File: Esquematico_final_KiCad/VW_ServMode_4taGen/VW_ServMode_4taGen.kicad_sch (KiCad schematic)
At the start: 33 parts, among them J1 MicroSDReader, J2 USB-C, J3 ClampConnections, J4 uC_custom, J5 TP4056_Custom_2extraOutputs, J6 3v3Switch, SW1 SW_In, SW2 SW_Out, SW3 SW_Reset

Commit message: - Esquematico actualizado - PCB enrutado
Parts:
- removed AFF2: LTS-6980HR, Display_7Segment:7SegmentLED_LTS6760_LTS6780, symbol Display_Character:LTS-6980HR
- removed D8: LED_ModServOn, symbol Device:LED
- removed D9: LED_ModServOff, symbol Device:LED
- removed J1: MicroSDReader, Connector_Wire:SolderWire-2sqmm_1x06_P7.8mm_D2mm_OD3.9mm, symbol Connector_Generic:Conn_01x06
- removed J2: USB-C, symbol Connector_Generic:Conn_01x04
- removed J3: ClampConnections, Connector_Hirose:Hirose_DF11-8DP-2DSA_2x04_P2.00mm_Vertical, symbol Connector_Generic:Conn_02x04_Counter_Clockwise
- removed J4: uC_custom, symbol Connector_Generic:Conn_02x15_Counter_Clockwise
- removed J5: TP4056_Custom_2extraOutputs, symbol Connector_Generic:Conn_02x04_Counter_Clockwise
- removed J6: 3v3Switch, symbol Connector_Generic:Conn_01x03
- removed SW3: SW_Reset, symbol Switch:SW_Push
- added AFF1: LTS-6960HR, Display_7Segment:7SegmentLED_LTS6760_LTS6780, symbol Display_Character:LTS-6960HR
- added BAR1: HDSP-4830_2, Display:HDSP-4830, symbol LED:HDSP-4830_2
- added BT1: Battery, Battery:BatteryHolder_Keystone_1042_1x18650, symbol Device:Battery_Cell
- added C1, C10, C11, C12, C15, C18, C2, C21, C22, C4, C6, C8: C100N, Capacitor_SMD:C_0603_1608Metric, symbol Device:C
- added C13, C14, C3, C5, C7, C9: C10U, Capacitor_SMD:C_0603_1608Metric, symbol Device:C
- added C16, C17: C4U7, Capacitor_SMD:C_0603_1608Metric, symbol Device:C
- added C19, C20: C20P, Capacitor_SMD:C_0603_1608Metric, symbol Device:C
- added H1, H2, H3, H4: MountingHole, MountingHole:MountingHole_3.2mm_M3, symbol Mechanical:MountingHole
- added J1: Conn_02x03_Counter_Clockwise, Connector_PinHeader_2.54mm:PinHeader_2x03_P2.54mm_Vertical, symbol Connector_Generic:Conn_02x03_Counter_Clockwise
- added J10: Micro_SD_Card, Own-Footprints:MicroSD_Memory, symbol Connector:Micro_SD_Card
- added J11: USB_C_Receptacle_USB2.0_14P, Connector_USB:USB_C_Receptacle_G-Switch_GT-USB-7010ASV, symbol Connector:USB_C_Receptacle_USB2.0_14P
- added J12: Conn_02x04_Counter_Clockwise, Connector_IDC:IDC-Header_2x04_P2.54mm_Horizontal, symbol Connector_Generic:Conn_02x04_Counter_Clockwise
- added J2: Conn_01x04_Pin, Connector_PinHeader_2.54mm:PinHeader_1x04_P2.54mm_Vertical, symbol Connector:Conn_01x04_Pin
- added J3, J4, J5, J6, J7: Conn_01x02_Pin, Connector_PinHeader_2.54mm:PinHeader_1x02_P2.54mm_Vertical, symbol Connector:Conn_01x02_Pin
- added Q1: IRLML6402, Package_TO_SOT_SMD:SOT-23, symbol Transistor_FET:IRLML6402
- added R1: R5K1, Resistor_SMD:R_0603_1608Metric, symbol Device:R
- added R12: R4K7, Resistor_SMD:R_0603_1608Metric, symbol Device:R
- added R15: R2K2, Resistor_SMD:R_0603_1608Metric, symbol Device:R
- added R21, R22, R23, R24, R25, RB1, RC1, RD1, RE1, RF1, RG1: R330, Resistor_SMD:R_0603_1608Metric, symbol Device:R
- added R26: R5K, Resistor_SMD:R_0603_1608Metric, symbol Device:R
- added R27: R15K, Resistor_SMD:R_0603_1608Metric, symbol Device:R
- added R30, R6, R7, R8, R9: R10K, Resistor_SMD:R_0603_1608Metric, symbol Device:R
- added R31, R32: R100K, Resistor_SMD:R_0603_1608Metric, symbol Device:R
- added R4: R1K, Resistor_SMD:R_0603_1608Metric, symbol Device:R
- added R5: R1K2, Resistor_SMD:R_0603_1608Metric, symbol Device:R
- added SW4: SW_Out, Button_Switch_SMD:SW_SPST_Omron_B3FS-105xP, symbol Switch:SW_Push
- added U1: TP4056, Package_SO:SOIC-8-1EP_3.9x4.9mm_P1.27mm_EP2.29x3mm, symbol tp4056:TP4056
- added U2: DW01, Package_TO_SOT_SMD:SOT-23-6_Handsoldering, symbol dw01:DW01
- added U3: FS8205A, Package_SO:TSSOP-8_4.4x3mm_P0.65mm, symbol fs8205:FS8205A
- added U4: AMS1117-3.3, Package_TO_SOT_SMD:SOT-223-3_TabPin2, symbol Regulator_Linear:AMS1117-3.3
- added U5: STM32F103C6Tx, Package_QFP:LQFP-48_7x7mm_P0.5mm, symbol MCU_ST_STM32F1:STM32F103C6Tx
- added Y1: Crystal, Crystal:Crystal_SMD_ECS_CSM3X-2Pin_7.6x4.1mm, symbol Device:Crystal
- D1: value LED_BAT25 -> PC13; footprint (none) -> LED_SMD:LED_0805_2012Metric
- D2: value LED_BAT50 -> BAT25; footprint (none) -> LED_THT:LED_D5.0mm
- D3: value LED_BAT75 -> BAT50; footprint (none) -> LED_THT:LED_D5.0mm
- D4: value LED_BAT99 -> BAT75; footprint (none) -> LED_THT:LED_D5.0mm
- D5: value LED_OK -> BAT99; footprint (none) -> LED_THT:LED_D5.0mm
- D6: value LED_ERROR -> LED; footprint (none) -> LED_THT:LED_D5.0mm
- D7: value LED_BAT0 -> LED; footprint (none) -> LED_THT:LED_D5.0mm
- R10, R11: value 1k -> R10K; footprint (none) -> Resistor_SMD:R_0603_1608Metric
- R13: value 330 -> R4K7; footprint (none) -> Resistor_SMD:R_0603_1608Metric
- R14: value 330 -> R47K; footprint (none) -> Resistor_SMD:R_0603_1608Metric
- R16: renamed from R12; value 330 -> R330; footprint (none) -> Resistor_SMD:R_0603_1608Metric
- R17: renamed from R4; value 330 -> R330; footprint (none) -> Resistor_SMD:R_0603_1608Metric
- R18: renamed from R5; value 330 -> R330; footprint (none) -> Resistor_SMD:R_0603_1608Metric
- R19: renamed from R6; value 330 -> R330; footprint (none) -> Resistor_SMD:R_0603_1608Metric
- R2: value 330 -> R5K1; footprint (none) -> Resistor_SMD:R_0603_1608Metric
- R20: renamed from R7; value 330 -> R330; footprint (none) -> Resistor_SMD:R_0603_1608Metric
- R28: renamed from R8; value 330 -> R10K; footprint (none) -> Resistor_SMD:R_0603_1608Metric
- R29: renamed from R9; value 330 -> R10K; footprint (none) -> Resistor_SMD:R_0603_1608Metric
- R3: value 330 -> R1K; footprint (none) -> Resistor_SMD:R_0603_1608Metric
- RA1: renamed from R1; value 330 -> R330; footprint (none) -> Resistor_SMD:R_0603_1608Metric
- SW1, SW2: footprint (none) -> Button_Switch_SMD:SW_SPST_Omron_B3FS-105xP
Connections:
- net LED_B0 is gone; now on net +5V: D7.2 (A)
- net SCL is gone; now on net +3V3: R10.2
- net SDA is gone; now on net +3V3: R11.2
- net +5V: now also D6.2 (A), C11.2, C3.2, C4.2, J11.A4 (VBUS), J11.A9 (VBUS), J11.B4 (VBUS), J11.B9 (VBUS), J4.1 (Pin_1), J6.1 (Pin_1), U1.4 (VCC), U1.8 (CE)
- net GND: now also R2.1, R29.1, C1.1, C10.1, C11.1, C13.1, C14.1, C15.1, C16.1, C18.1, C19.1, C2.1, C20.1, C3.1, C4.1, C5.1, C6.1, C7.1, C8.1, C9.1, J1.5 (Pin_5), J1.6 (Pin_6), J10.6 (VSS), J11.A1 (GND), J11.A12 (GND), J11.B1 (GND), J11.B12 (GND), J12.4 (Pin_4), J2.4 (Pin_4), J4.2 (Pin_2), J5.2 (Pin_2), J6.2 (Pin_2), J7.2 (Pin_2), R1.2, R22.2, R23.2, R24.2, R25.2, R27.1, R5.1, SW4.1, U1.1 (TEMP), U1.3 (GND), U4.1 (GND), U5.23 (VSS), U5.35 (VSS), U5.47 (VSS), U5.8 (VSSA); no longer R13.2, R14.2, R2.2, R29.2, R3.2, RA1.1
- net LED_A: now also RA1.2, U5.14 (PA4)
- net LED_B: now also RB1.2, U5.13 (PA3)
- net LED_B25: now also BAR1.7 (A), BAR1.8 (A), U5.21 (PB10); no longer D1.2 (A)
- net LED_B50: now also BAR1.5 (A), BAR1.6 (A), U5.22 (PB11); no longer D2.2 (A)
- net LED_B75: now also BAR1.3 (A), BAR1.4 (A), U5.29 (PA8); no longer D3.2 (A)
- net LED_B99: now also BAR1.1 (A), BAR1.2 (A), U5.30 (PA9); no longer D4.2 (A)
- net LED_C: now also RC1.2, U5.10 (PA0)
- net LED_D: now also RD1.2, U5.12 (PA2)
- net LED_E: now also RE1.2, U5.11 (PA1)
- net LED_ERROR: now also D3.2 (A), U5.25 (PB12); no longer D6.2 (A)
- net LED_F: now also RF1.2, U5.40 (PB4)
- net LED_G: now also RG1.2, U5.39 (PB3)
- net LED_OK: now also D2.2 (A), U5.26 (PB13); no longer D5.2 (A)
- net TP_B-: now also BT1.2 (-), C12.1, U2.6 (GND), U3.2 (S1), U3.3 (S1)
- net CONN_SCL: now reaches R13.1
- net CONN_SCL: now also J12.6 (Pin_6), U5.42 (PB6)
- net at D5.1 (K): now also R25.1; no longer R2.1
- net at R14.1: now also C17.1, Q1.1 (G), R15.1
- net at R16.1: now also BAR1.11 (K), BAR1.12 (K); no longer D7.1 (K)
- net at R18.1: now also BAR1.15 (K), BAR1.16 (K); no longer D2.1 (K)
- net SD_CS: now reaches R11.1
- net SD_CS: now also J10.2 (DAT3/CD), U5.4 (PC15); no longer R10.1
- net at D6.1 (K): now also R3.2; no longer R3.1
- net at R19.1: now also BAR1.17 (K), BAR1.18 (K); no longer D3.1 (K)
- net at R17.1: now also BAR1.13 (K), BAR1.14 (K); no longer D1.1 (K)
- net at R20.1: now also BAR1.19 (K), BAR1.20 (K); no longer D4.1 (K)
- net +3.3V renamed +3V3
- net +3V3: now also D1.2 (A), R14.2, AFF1.3 (C.A.), AFF1.8 (C.A.), C1.2, C10.2, C14.2, C15.2, C17.2, C2.2, C21.2, C22.2, C5.2, C6.2, C9.2, J1.1 (Pin_1), J1.2 (Pin_2), J10.4 (VDD), J2.1 (Pin_1), J5.1 (Pin_1), J7.1 (Pin_1), Q1.2 (S), R30.2, R8.2, R9.2, U4.2 (VO), U5.24 (VDD), U5.36 (VDD), U5.48 (VDD), U5.9 (VDDA)
- net Push_In renamed PUSH_IN
- net PUSH_IN: now also C21.1, U5.28 (PB15)
- net Push_Out renamed PUSH_OUT
- net PUSH_OUT: now also R29.2, C22.1, U5.27 (PB14); no longer R29.1
- new net: AFF1.4 (c), RC1.1
- new net: AFF1.1 (e), RE1.1
- new net: AFF1.10 (g), RG1.1
- new net: AFF1.2 (d), RD1.1
- new net: AFF1.6 (b), RB1.1
- new net: AFF1.7 (a), RA1.1
- new net: AFF1.9 (f), RF1.1
- new net: D2.1 (K), R22.1
- new net: J11.A5 (CC1), R1.1
- new net: D4.1 (K), R24.1
- new net: R5.2, U1.2 (PROG)
- new net: J11.B5 (CC2), R2.2
- new net: D7.1 (K), R4.2
- new net: R6.1, U3.6 (S2), U3.7 (S2)
- new net: R6.2, U2.2 (CS)
- new net: U2.1 (OD), U3.4 (G1)
- new net: U2.3 (OC), U3.5 (G2)
- new net: C12.2, R7.2, U2.5 (VCC)
- new net: R31.1, U5.44 (BOOT0)
- new net: D3.1 (K), R23.1
- new net: D1.1 (K), R21.1
- new net #RESET: R30.1, SW4.2, U5.7 (NRST)
- new net BAT+: BT1.1 (+), C13.2, J3.2 (Pin_2), R26.2, R7.1, U1.5 (BAT)
- new net BAT_LVL: C18.2, R26.1, R27.2, U5.18 (PB0)
- new net BOOT0: J1.3 (Pin_3), R31.2
- new net BOOT1: J1.4 (Pin_4), R32.2
- new net CONN_SDA: J12.5 (Pin_5), R12.1, U5.43 (PB7)
- new net DCLK: J2.3 (Pin_3), U5.37 (PA14)
- new net DIO: J2.2 (Pin_2), U5.34 (PA13)
- new net DO_3V3: C16.2, J12.8 (Pin_8), Q1.3 (D), R12.2, R13.2
- new net DO_CONTROL3V3: R15.2, U5.19 (PB1)
- new net LED_B00: BAR1.10 (A), BAR1.9 (A), R32.1, U5.20 (PB2)
- new net LED_MODSERV_OFF: D5.2 (A), U5.3 (PC14)
- new net LED_MODSERV_ON: D4.2 (A), U5.31 (PA10)
- new net OSC8M_IN: C20.2, U5.6 (PD1), Y1.1
- new net OSC8M_OUT: C19.2, U5.5 (PD0), Y1.2
- new net PC13: R21.2, U5.2 (PC13)
- new net SD_CLK: J10.5 (CLK), R9.1, U5.15 (PA5)
- new net SD_MISO: J10.7 (DAT0), R8.1, U5.16 (PA6)
- new net SD_MOSI: J10.3 (CMD), R10.1, U5.17 (PA7)
- new net SHIELD: J10.9 (SHIELD), J11.S1 (SHIELD)
- new net TP_#CHRG: R3.1, U1.7 (~{CHRG}), U5.46 (PB9)
- new net TP_#STDBY: R4.1, U1.6 (~{STDBY}), U5.45 (PB8)
- new net USB_D+: J11.A6 (D+), J11.B6 (D+), U5.33 (PA12)
- new net USB_D-: J11.A7 (D-), J11.B7 (D-), U5.32 (PA11)
- new net VIN+: C7.2, C8.2, J3.1 (Pin_1), U4.3 (VI)
- no-connect marks 0 -> 14
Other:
- note added: "Battery Charger"
- note added: "Battery Level"
- note added: "Cada led con su resistencia"
- note added: "Connector IDC BOX"
- note added: "Error code"
- note added: "IMPORTANTE: DO_CONTROL3V3 es una salida lógica del uC de 3.3v. Hacer un circuito básico que controle el paso o corte de voltaje aquí. Casi siempre estará cortado y sólo se permitirá el voltaje por máximo 10 segundos continuos. UPDATE: DO_3V3 es la linea de +3.3v controlada por el uC. Un Mosfet canal P controla la salida positiva de +3.3V Su control require lógica inversa: 1 lógico = DO_3V3 esta d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"
- note added: "IMPORTANTE: En el diseño final estos elementos estarán en la capa de ABAJO: - Lector de MicroSD - Push Reset (la idea es que se presione con un palillo por un agujero)"
- note added: "IMPORTANTE: NO olvidar indicar en PCB hacia dónde BOOT0 y BOOT1 son 1 lógico y 0 lógico."
- note added: "IMPORTANTE: Para TP_B- y TP_B+ dejar headers para soldar los cables de la batería. UPDATE: Se usará un socket porta baterías para baterías 18650"
- note added: "IMPORTANTE: Si el microSD no aparece como componente se puede armar, sólo ocupa 4 resistencia y 2 capacitores (y el sócalo). UPDATE: El footprint de la microSD no aparece y se tendrá que dibujar de acuerdo al componente elegido."
- note added: "Indicators"
- note added: "JTAG"
- note added: "MicroSD CARD"
- note added: "Microcontroller"
- note added: "NOTA: J3 son orificios para soldar un interruptor con cables. Puede venir soldado o no, dependera del diseño final."
- note added: "Notas de diseño"
- note added: "Oscillators"
- note added: "PREGUNTA: Este conector JTAG debería estar a 90 grados como la placa original del STM32? idealmente no debería venir soldado"
- note added: "Power Supply"
- note added: "Push Buttons"
- note added: "Screws"
- note added: "Se pone este arreglo para tener máximo 3.15V cuando la batería esta completamente cargada"
- note added: "Selection"
- note removed: "GND del USB-C"
- note removed: "IMPORTANTE: DO_5V es una salida lógica del uC de 3.3v. Hacer un circuito básico que controle el paso o corte de voltaje aquí. Casi siempre estará cortado y sólo se permitirá el voltaje por máximo 10 segundos continuos. Se puede usar un Relé, MOSFET lógico, transistor, o lo que haya."
- note removed: "IMPORTANTE: En el diseño final estos elemntos estarán en la capa de ABAJO: - Lector de MicroSD - Push Reset (la idea es que se presione con un palillo por un agujero)"
- note removed: "IMPORTANTE: Este botón es parte del esquematico original del STM32. Puedes extender sus terminales a otro lugar y poner un PUSH o puedes dejar este push para reiniciar el micro. Recuerda que se debe presionar con un palo y a veces es metálico así que podrían hacer corto en algún lado."
- note removed: "IMPORTANTE: Para TP_B- y TP_B+ dejar headers para soldar los cables de la batería."
- note removed: "IMPORTANTE: Poner un regulador a la entrada de 3V3 y GND para el uC"
- note removed: "IMPORTANTE: Si el microSD no aparece como componente se puede armar, sólo ocupa 4 resistencia y 2 capacitores (y el sócalo)."
- note removed: "VCC del USB-C"
- title: (none) -> VW_ServMode_4taGen
- moved on the sheet: R16, R17, R18, R19, R20, R28, R29, RA1, SW1, SW2

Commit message: - BOM actualizado - Gerbers generados
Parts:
- D2: value BAT25 -> D_OK
- D3: value BAT50 -> D_ERR
- D4: value BAT75 -> D_MSON
- D5: value BAT99 -> D_MSOFF
- R26: value R5K -> R5K1
- U3: footprint Package_SO:TSSOP-8_4.4x3mm_P0.65mm -> Package_TO_SOT_SMD:SOT-23-6_Handsoldering
- U5: value STM32F103C6Tx -> STM32F103C8T6
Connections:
- net CONN_SDA: now also J12.8 (Pin_8); no longer J12.5 (Pin_5)
- net DO_3V3: now also J12.2 (Pin_2); no longer J12.8 (Pin_8)
- net GND: now also J12.7 (Pin_7), R6.1, U3.3 (S2); no longer J12.4 (Pin_4)
- net TP_B-: now also U3.1 (S1); no longer U3.2 (S1), U3.3 (S1)
- net at U2.1 (OD): now also U3.6 (G1); no longer U3.4 (G1)
- net at U2.3 (OC): now also U3.4 (G2); no longer U3.5 (G2)
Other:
- moved on the sheet: D5, J12, R25

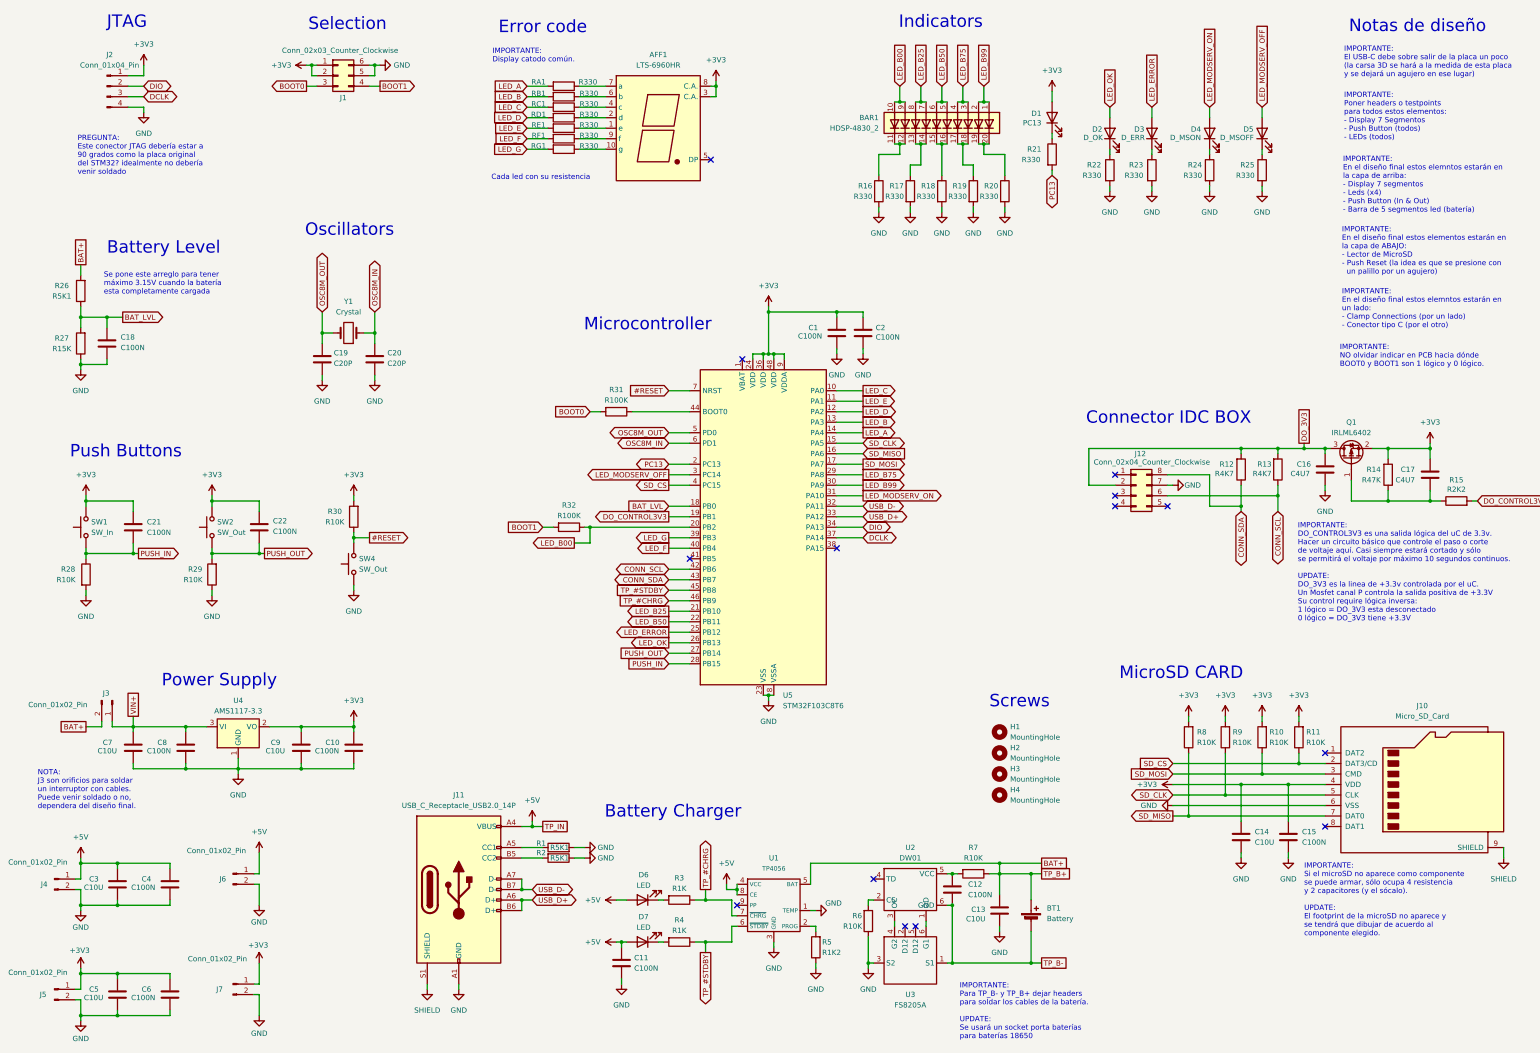
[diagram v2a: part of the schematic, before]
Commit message: Errores corregidos - Resistencias en bus usb, leds cerca de usb, leds de nivel de batería
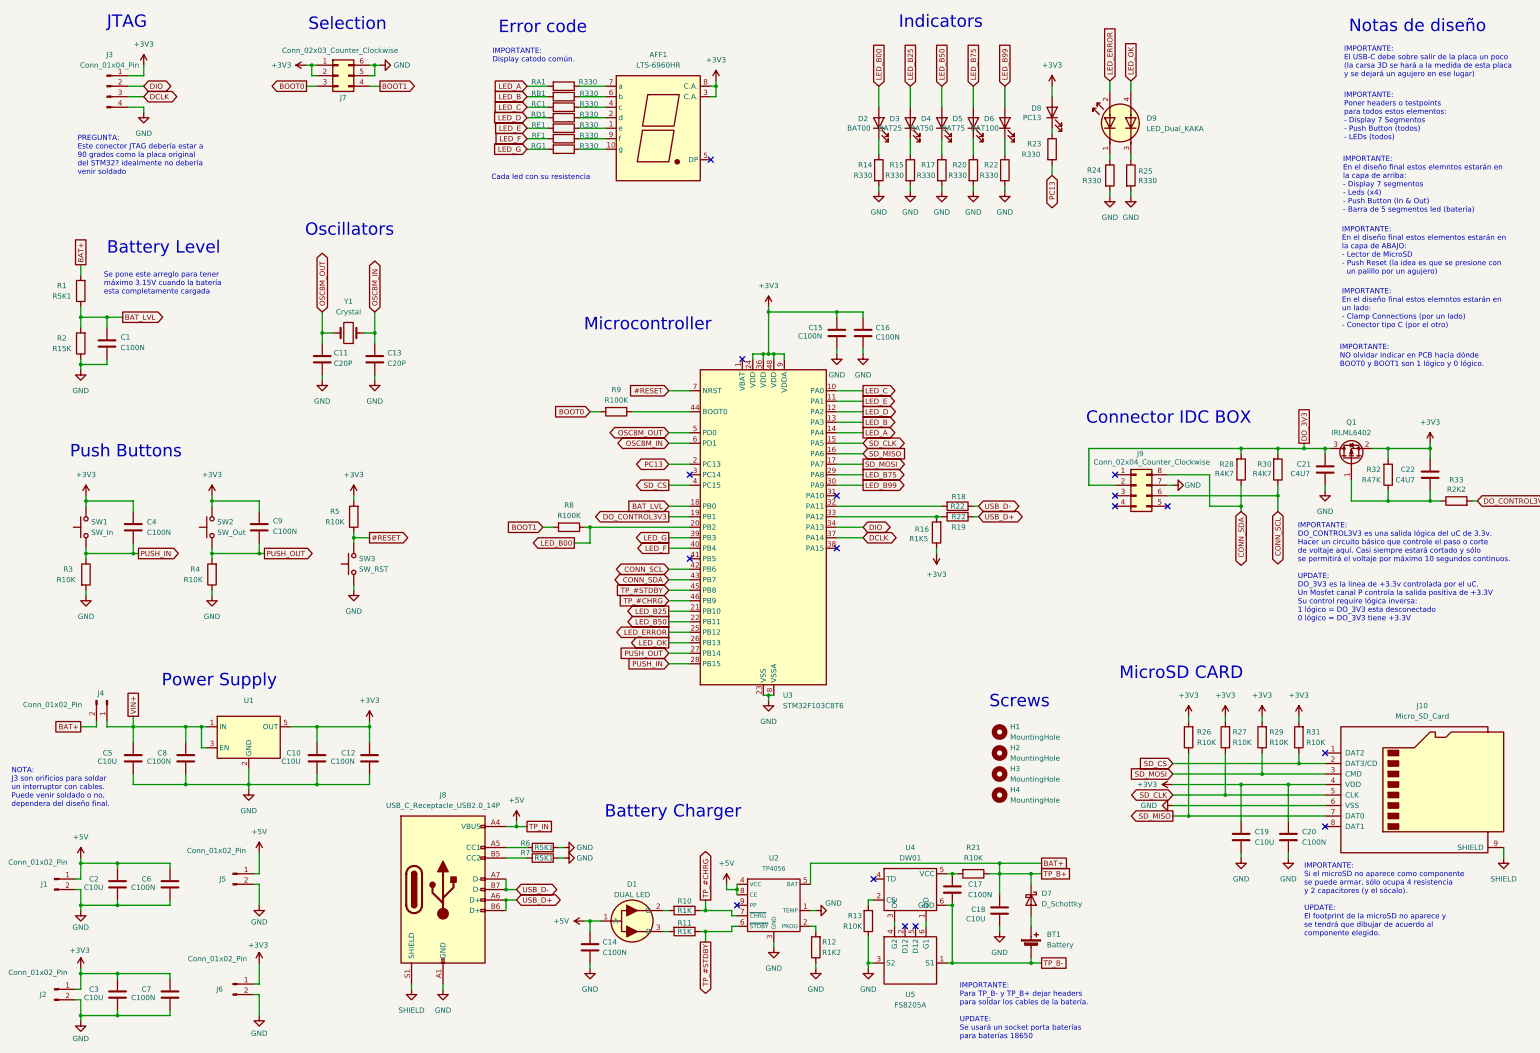
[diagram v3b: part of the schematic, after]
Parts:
- removed BAR1: HDSP-4830_2, Display:HDSP-4830, symbol LED:HDSP-4830_2
- removed D7: LED, LED_THT:LED_D5.0mm, symbol Device:LED
- removed R24, R25: R330, Resistor_SMD:R_0603_1608Metric, symbol Device:R
- removed U4: AMS1117-3.3, Package_TO_SOT_SMD:SOT-223-3_TabPin2, symbol Regulator_Linear:AMS1117-3.3
- added D1: DUAL LED, JCU_LED_SMD:1204 DUAL LED, symbol JCU_LED_SMD:A-SP1102DR6GHC-C01-2C
- added D7: D_Schottky, symbol Device:D_Schottky
- added D9: LED_Dual_KAKA, JCU_LED_SMD:0805 DUAL LED, symbol Device:LED_Dual_KAKA
- added R16: R1K5, Resistor_SMD:R_0603_1608Metric, symbol Device:R
- added R18, R19: R22, Resistor_SMD:R_0603_1608Metric, symbol Device:R
- added U1: ~, Package_SO:TSOP-5_1.65x3.05mm_P0.95mm, symbol JCU_PowerSupply:NCP115ASN330T2G
- D2: value D_OK -> BAT00; footprint LED_THT:LED_D5.0mm -> LED_SMD:LED_0603_1608Metric
- D3: value D_ERR -> BAT25; footprint LED_THT:LED_D5.0mm -> LED_SMD:LED_0603_1608Metric
- D4: value D_MSON -> BAT50; footprint LED_THT:LED_D5.0mm -> LED_SMD:LED_0603_1608Metric
- D5: value D_MSOFF -> BAT75; footprint LED_THT:LED_D5.0mm -> LED_SMD:LED_0603_1608Metric
- D6: value LED -> BAT100; footprint LED_THT:LED_D5.0mm -> LED_SMD:LED_0603_1608Metric
- SW3: renamed from SW4; value SW_Out -> SW_RST
- renumbered C18 to C1, C9 to C10, C19 to C11, C10 to C12, C20 to C13, C11 to C14, C1 to C15, C2 to C16, C12 to C17, C13 to C18, C14 to C19, C3 to C2, C15 to C20, C16 to C21, C17 to C22, C5 to C3, C21 to C4, C7 to C5, C4 to C6, C6 to C7, C22 to C9, D1 to D8, J4 to J1, J5 to J2, J2 to J3, J3 to J4, J6 to J5, J7 to J6, J1 to J7, J11 to J8, J12 to J9, R26 to R1, R3 to R10, R4 to R11, R5 to R12, R6 to R13, R16 to R14, R17 to R15, R18 to R17, R27 to R2, R19 to R20, R7 to R21, R20 to R22, R21 to R23, R22 to R24, R23 to R25, R8 to R26, R9 to R27, R12 to R28, R10 to R29, R28 to R3, R13 to R30, R11 to R31, R14 to R32, R15 to R33, R29 to R4, R30 to R5, R1 to R6, R2 to R7, R32 to R8, R31 to R9, U1 to U2, U5 to U3, U2 to U4, U3 to U5
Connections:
- net +3V3: now also R16.1, U1.5 (OUT)
- net +5V: now also D1.1 (A); no longer D6.2 (A)
- net BAT+: now also D7.1 (K); no longer BT1.1 (+)
- net GND: now also U1.2 (GND), U1.5 (OUT)
- net LED_B00: now also D2.2 (A)
- net LED_B25: now also D3.2 (A)
- net LED_B50: now also D4.2 (A)
- net LED_B75: now also D5.2 (A)
- net LED_B99: now also D6.2 (A)
- net LED_ERROR: now also D9.2 (A1); no longer D3.2 (A)
- net LED_OK: now also D9.4 (A2); no longer D2.2 (A)
- net USB_D+: now also R19.1; no longer U3.33 (PA12)
- net USB_D-: now also R18.1; no longer U3.32 (PA11)
- net VIN+: now also U1.1 (IN), U1.3 (EN)
- net at D5.1 (K): now also R20.1
- net at R14.1: now also D2.1 (K)
- net at R15.1: now also D3.1 (K)
- net at R17.1: now also D4.1 (K)
- net at R22.1: now also D6.1 (K)
- net at R24.1: now also D9.1 (K1); no longer D2.1 (K)
- net at R10.2: now also D1.2 (G); no longer D6.1 (K)
- net at R11.2: now also D1.3 (R)
- net at R25.1: now also D9.3 (K2); no longer D3.1 (K)
- net LED_MODSERV_OFF: no longer names the net of U3.3 (PC14)
- net LED_MODSERV_OFF: no longer D5.2 (A)
- net LED_MODSERV_ON: no longer names the net of U3.31 (PA10)
- net LED_MODSERV_ON: no longer D4.2 (A)
- new net: BT1.1 (+), D7.2 (A)
- new net: R18.2, U3.32 (PA11)
- new net: R16.2, R19.2, U3.33 (PA12)
- no-connect marks 14 -> 16
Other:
- moved on the sheet: BT1, C10, C12, C14, C5, C8, D8, J4, J8, R10, R11, R14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

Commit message: Segunda version finalizada
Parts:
- removed D1: DUAL LED, JCU_LED_SMD:1204 DUAL LED, symbol JCU_LED_SMD:A-SP1102DR6GHC-C01-2C
- removed D7: D_Schottky, symbol Device:D_Schottky
- removed D9: LED_Dual_KAKA, JCU_LED_SMD:0805 DUAL LED, symbol Device:LED_Dual_KAKA
- added D1: LED Dual Common Anode, JCU_LED_SMD:SMD,2x3mm, symbol JCU_LED_SMD:12-22/BHR6C-A01/2C
- added D7: LED Dual Independient, JCU_LED_SMD:SMD-4P,3.5x2.8mm, symbol JCU_LED_SMD:A-SC6302R6AGHC-A03-2T
- AFF1: JLCPCB Part #  (none) -> C8092
- BT1: JLCPCB Part # (none) -> C2988620
- D2, D3, D4, D5, D6: footprint LED_SMD:LED_0603_1608Metric -> LED_THT:LED_Rectangular_W5.0mm_H2.0mm
- U1: value ~ -> NCP115
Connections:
- net +5V: now also D1.1 (A)
- net BAT+: now also BT1.1 (+)
- net LED_ERROR: now also D7.1 (AR)
- net LED_OK: now also D7.3 (AG)
- net at R24.1: now also D7.4 (KR)
- net at R25.1: now also D7.2 (KG)
- net at R10.2: now also D1.2 (R)
- net at R11.2: now also D1.3 (B)
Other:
- moved on the sheet: BT1, R24
